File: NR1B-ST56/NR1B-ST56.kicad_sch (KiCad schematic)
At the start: 13 parts, among them J1 Conn_02x04_Odd_Even, J2 Conn_02x04_Odd_Even, J3 Conn_01x02, U1 S29GL01GP, U2 DG419LDY, X1 NUCLEO144-ZIO

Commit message: NR1B-ST56 1.0 RC 1
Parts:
- added C4: 0.1uF, Capacitor_SMD:C_0805_2012Metric, symbol Device:C
- added C5: 47uF 16V, Capacitor_SMD:CP_Elec_5x5.3, symbol Device:C_Polarized_US
- added D1, D3, D5: S1G, Diode_SMD:D_SOD-323, symbol Device:D
- added D2, D6: 15V, Diode_SMD:D_SOD-323, symbol Device:D_Zener
- added D4: 5.1V, Diode_SMD:D_SOD-323, symbol Device:D_Zener
- added FID1, FID2, FID3: Fiducial, Fiducial:Fiducial_0.5mm_Mask1mm, symbol Mechanical:Fiducial
- added R4: 1M, Resistor_SMD:R_0805_2012Metric, symbol Device:R
- added U3: OPA189ID, Package_SO:SOIC-8_3.9x4.9mm_P1.27mm, symbol NISoC-Socket:OPA189ID
- J1, J2: value Conn_02x04_Odd_Even -> 0.1" Female Long Tail
- X1: MPN (none) -> Nucleo-144; Manufacturer (none) -> ST Micro
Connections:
- net +12V: now also C4.1, D1.1 (K), D2.1 (K), U3.7 (V+); no longer J2.6 (Pin_6)
- net ANA_VWL: now also R4.1, U3.3 (+); no longer U1.14 (~{RESET})
- net EVIO: now also D5.1 (K), D6.1 (K); no longer J3.1 (Pin_1)
- net GND: now also C4.2, C5.2, D2.2 (A), D4.2 (A), D6.2 (A), R4.2, U3.4 (V-)
- net VCC: now also C5.1, D3.1 (K), D4.1 (K); no longer X1.16 (+3V3)
- new net 12V_IN: D1.2 (A), J2.6 (Pin_6)
- new net EVIO_IN: D5.2 (A), J3.1 (Pin_1)
- new net VCC_IN: D3.2 (A), X1.16 (+3V3)
- new net Vwl_buf: U1.14 (~{RESET}), U3.2 (-), U3.6
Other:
- note added: "CE Switch"
- note added: "CE switch allows for regular operation via NE1, or V read via ANA_CE."
- note added: "Connectors"
- note added: "Detector Interface"
- note added: "Forward diodes for reverse-voltage protection. Zeners for overvoltage protection."
- note added: "Jumper JP1 1-2 for VIO=VCC. Jumper JP1 2-3 for VIO=Ext. VIO Supply ext. VIO on J3"
- note added: "Optional discharge resistor"
- note added: "Power Protection"
- note added: "Vwl buffer"
- note removed: "+15V"
- note removed: "+5V"
- note removed: "-15V"
- note removed: "24V"
- note removed: "Jumper JP1 1-2 for VIO=VCC. Jumper JP1 2-3 for VIO=Vext. Supply ext. VIO on J3"
- title: NISoC Readout 1 Module Base -> NISoC Readout 1 Module - Socket TSOP-56 Bus
- moved on the sheet: C1, C2, C3, J1, J2, J3, JP1, R1, R2, R3, U1, U2A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

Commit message: Added 9V for CE#; Made global labels hierarchical
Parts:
- removed U3: OPA189ID, Package_SO:SOIC-8_3.9x4.9mm_P1.27mm, symbol NISoC-Socket:OPA189ID
- added C6: 0.33uF, Capacitor_SMD:C_0805_2012Metric, symbol Device:C
- added C7: 0.1uF, Capacitor_SMD:C_0805_2012Metric, symbol Device:C
- added D7: S1G, Diode_SMD:D_SOD-323, symbol Device:D
- added D8: 18V, Diode_SMD:D_SOD-323, symbol Device:D_Zener
- added NT1, NT2: NetTie_2, NetTie:NetTie-2_SMD_Pad0.5mm, symbol Device:NetTie_2
- added R5: 1M, Resistor_SMD:R_0805_2012Metric, symbol Device:R
- added U3: OPA2189ID, Package_SO:SOIC-8_3.9x4.9mm_P1.27mm, symbol NISoC-Socket:OPA2189ID
- added U4: NCV7800, Package_TO_SOT_SMD:TO-263-3_TabPin2, symbol NISoC-Socket:NCV7800
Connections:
- net +12V: now also U3.8 (V+)
- net ANA_CE: now also C7.1, U4.3 (OUT); no longer J1.8 (Pin_8)
- net ANA_VWL: now also NT1.1, U3.3 (+)
- net ANA_WP: now also J1.3 (Pin_3), NT2.1, R5.1, U3.5 (+); no longer J1.5 (Pin_5), U1.16 (~{WP}/ACC)
- net GND: now also C6.2, C7.2, D8.2 (A), R5.2, U3.4 (V-), U4.2 (GND)
- net +15V_IN: now reaches J2.2 (Pin_2)
- net +15V_IN: now also D7.2 (A)
- net ANA_WP_SENSE: now reaches J1.1 (Pin_1)
- net ANA_WP_SENSE: now also NT2.2
- net Vwl_buf renamed VWL_BUF
- net VWL_BUF: now also U3.1, U3.2 (-)
- new net +15V: C6.1, D7.1 (K), D8.1 (K), U4.1 (IN)
- new net ANA_VWL_SENSE: J1.5 (Pin_5), NT1.2
- new net WP_BUF: U1.16 (~{WP}/ACC), U3.6 (-), U3.7
- no-connect marks 86 -> 84
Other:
- note added: "WP buffer"
- note added: "~{CE} 9V output to enter V read mode"
- moved on the sheet: C1, C2, C3, C4, J1, J2, J3, JP1, R1, R2, R4, U2A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

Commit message: Many updates
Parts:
- removed D1: S1G, Diode_SMD:D_SOD-323, symbol Device:D
- removed D2: 15V, Diode_SMD:D_SOD-323, symbol Device:D_Zener
- added D10: 18V, Diode_SMD:D_SOD-323, symbol Device:D_Zener
- added D9: S1G, Diode_SMD:D_SOD-323, symbol Device:D
- added R6, R7: 1K, Resistor_SMD:R_0805_2012Metric, symbol Device:R
- U2: MFG 1 (none) -> Maxim; MPN 1 (none) -> DG419LDY
- U3: footprint Package_SO:SOIC-8_3.9x4.9mm_P1.27mm -> Package_SO:VSSOP-8_3.0x3.0mm_P0.65mm
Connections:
- net +12V is gone; now on net +15V: C4.1, U2.4 (V+), U3.8 (V+)
- net GND: now also D10.1 (K), R7.2; no longer C4.2, U3.4 (V-)
- net WP_BUF: now also R6.2; no longer U3.6 (-)
- net -15V_IN: now reaches J2.1 (Pin_1)
- net -15V_IN: now also D9.1 (K)
- net 12V_IN: no longer names the net of J2.6 (Pin_6)
- new net: R6.1, R7.1, U3.6 (-)
- new net -15V: C4.2, D10.2 (A), D9.2 (A), U3.4 (V-)

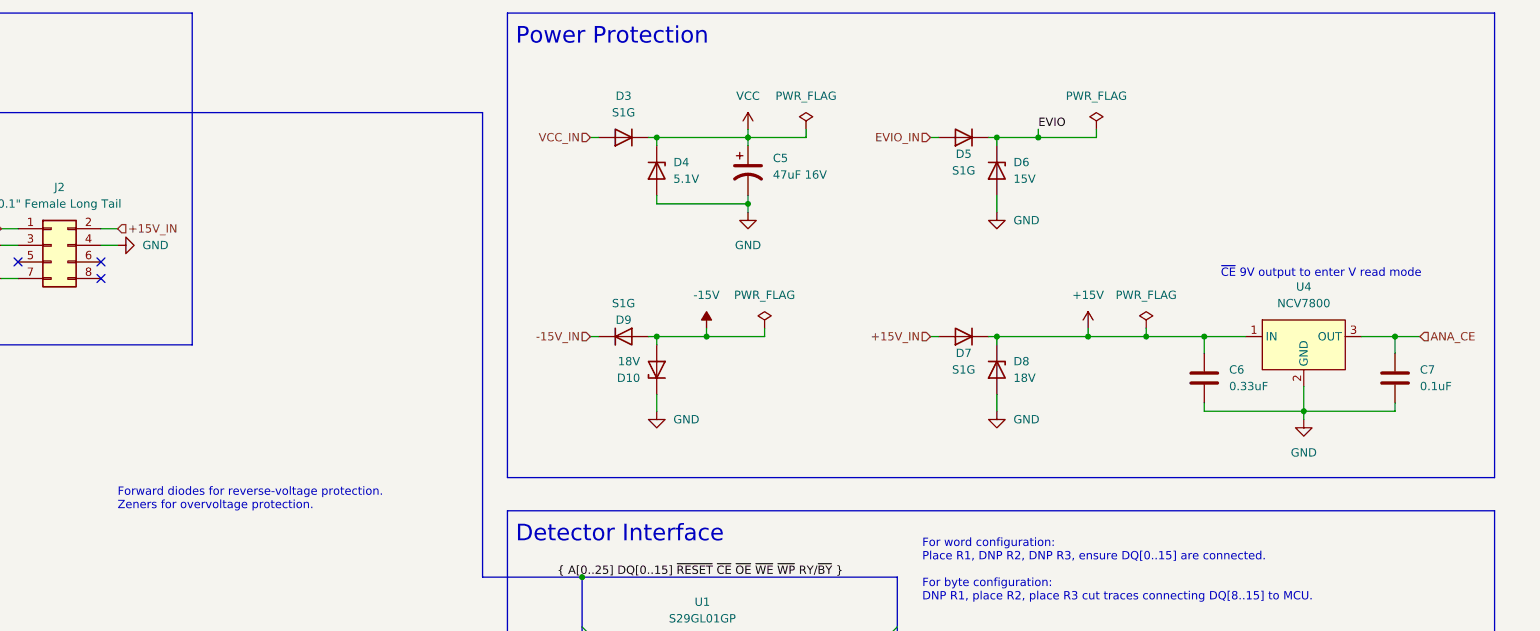
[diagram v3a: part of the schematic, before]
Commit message: Fixed footprints and silkscreen
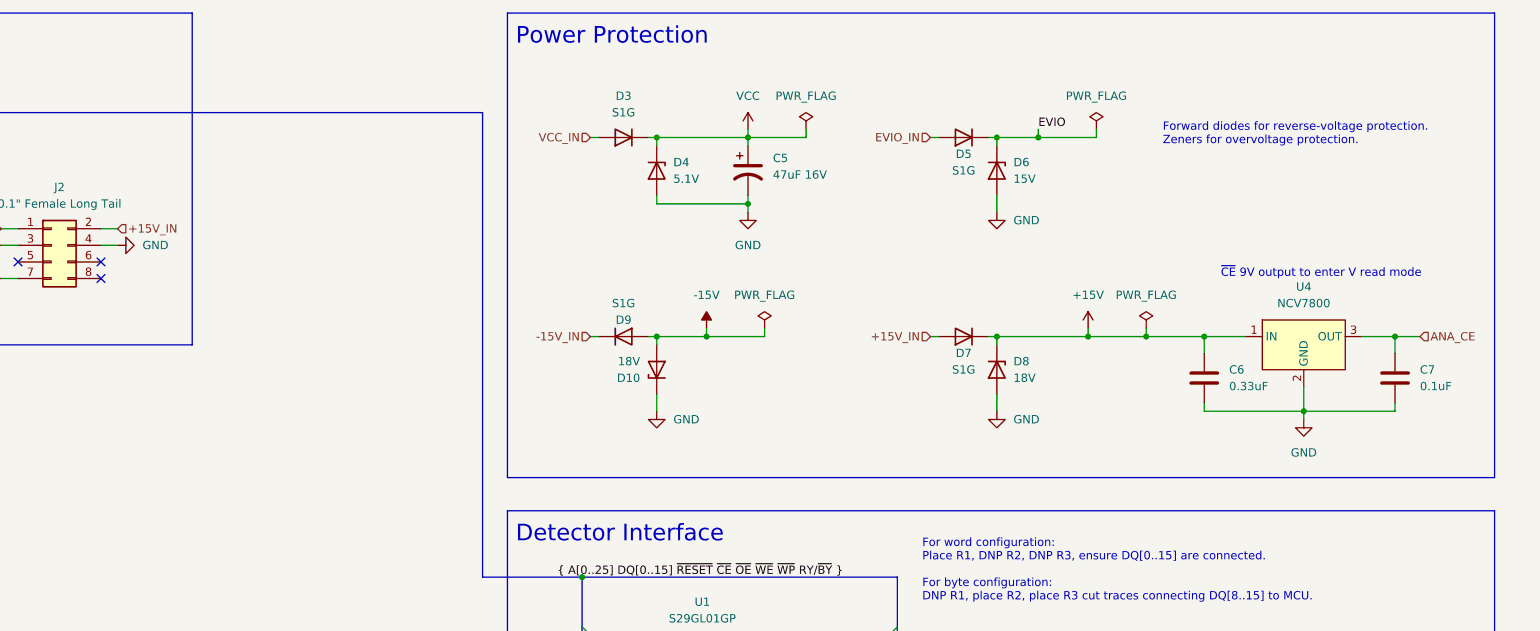
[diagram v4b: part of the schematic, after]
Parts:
- D3, D5, D7, D9: footprint Diode_SMD:D_SOD-323 -> Diode_SMD:D_SMA
- R6, R7: footprint Resistor_SMD:R_0805_2012Metric -> Resistor_SMD:R_0603_1608Metric
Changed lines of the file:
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@@
   (title_block
     (title "NISoC Readout 1 Module - Socket TSOP-56 Bus")
-    (date "2022-07-11")
+    (date "2022-08-02")
     (rev "1.0")
     (company "University of Dallas")
@@
   )
   (text "Forward diodes for reverse-voltage protection.\nZeners for overvoltage protection."
-    (at 198.12 93.98 0)
+    (at 358.14 38.1 0)
     (effects (font (size 1.27 1.27)) (justify left bottom))
   )
@@
     (property "Reference" "D3" (id 0) (at 275.59 30.48 0))
     (property "Value" "S1G" (id 1) (at 275.59 33.02 0))
-    (property "Footprint" "Diode_SMD:D_SOD-323" (id 2) (at 275.59 36.83 0)
+    (property "Footprint" "Diode_SMD:D_SMA" (id 2) (at 275.59 36.83 0)
       (effects (font (size 1.27 1.27)) hide)
     )
@@
     (property "Reference" "D5" (id 0) (at 327.66 39.37 0))
     (property "Value" "S1G" (id 1) (at 327.66 41.91 0))
-    (property "Footprint" "Diode_SMD:D_SOD-323" (id 2) (at 327.66 36.83 0)
+    (property "Footprint" "Diode_SMD:D_SMA" (id 2) (at 327.66 36.83 0)
       (effects (font (size 1.27 1.27)) hide)
     )
@@
     (property "Reference" "R6" (id 0) (at 341.63 179.07 90))
     (property "Value" "1K" (id 1) (at 341.63 173.99 90))
-    (property "Footprint" "Resistor_SMD:R_0805_2012Metric" (id 2) (at 341.63 174.752 90)
+    (property "Footprint" "Resistor_SMD:R_0603_1608Metric" (id 2) (at 341.63 174.752 90)
       (effects (font (size 1.27 1.27)) hide)
     )
@@
     (property "Reference" "D9" (id 0) (at 275.59 64.77 0))
     (property "Value" "S1G" (id 1) (at 275.59 62.23 0))
-    (property "Footprint" "Diode_SMD:D_SOD-323" (id 2) (at 275.59 67.31 0)
+    (property "Footprint" "Diode_SMD:D_SMA" (id 2) (at 275.59 67.31 0)
       (effects (font (size 1.27 1.27)) hide)
     )
@@
       (effects (font (size 1.27 1.27)) (justify left))
     )
-    (property "Footprint" "Resistor_SMD:R_0805_2012Metric" (id 2) (at 353.822 181.61 90)
+    (property "Footprint" "Resistor_SMD:R_0603_1608Metric" (id 2) (at 353.822 181.61 90)
       (effects (font (size 1.27 1.27)) hide)
     )
@@
     (property "Reference" "D7" (id 0) (at 327.66 69.85 0))
     (property "Value" "S1G" (id 1) (at 327.66 72.39 0))
-    (property "Footprint" "Diode_SMD:D_SOD-323" (id 2) (at 327.66 67.31 0)
+    (property "Footprint" "Diode_SMD:D_SMA" (id 2) (at 327.66 67.31 0)
       (effects (font (size 1.27 1.27)) hide)
     )
@@
     )
     (path "/242da293-ae6d-46dd-a6b6-d6ba3d1de6fe"
-      (reference "D3") (unit 1) (value "S1G") (footprint "Diode_SMD:D_SOD-323")
+      (reference "D3") (unit 1) (value "S1G") (footprint "Diode_SMD:D_SMA")
     )
     (path "/9b3a8a31-780a-470f-af9f-a3d21756d3b6"
@@
     )
     (path "/63e71f4d-a796-4447-8c82-09fd88a5d9bf"
-      (reference "D5") (unit 1) (value "S1G") (footprint "Diode_SMD:D_SOD-323")
+      (reference "D5") (unit 1) (value "S1G") (footprint "Diode_SMD:D_SMA")
     )
     (path "/a94e8f9e-afa6-4830-aa93-22a913360207"
@@
     )
     (path "/f299b552-8ee7-4386-9f69-6d096e2c001a"
-      (reference "D7") (unit 1) (value "S1G") (footprint "Diode_SMD:D_SOD-323")
+      (reference "D7") (unit 1) (value "S1G") (footprint "Diode_SMD:D_SMA")
     )
     (path "/61e67969-2acc-4271-bd67-f08a12f7e9a7"
@@
     )
     (path "/b0782c9b-6f78-48ad-ae89-fb24252cf241"
-      (reference "D9") (unit 1) (value "S1G") (footprint "Diode_SMD:D_SOD-323")
+      (reference "D9") (unit 1) (value "S1G") (footprint "Diode_SMD:D_SMA")
     )
     (path "/c7a096df-9a13-41ae-ae08-3eb578cfc15d"
@@
     )
     (path "/ad5cafb3-1aba-4113-8611-9bc359308370"
-      (reference "R6") (unit 1) (value "1K") (footprint "Resistor_SMD:R_0805_2012Metric")
+      (reference "R6") (unit 1) (value "1K") (footprint "Resistor_SMD:R_0603_1608Metric")
     )
     (path "/de0b3ff5-56b8-4e0c-af8a-6e6e370d3733"
-      (reference "R7") (unit 1) (value "1K") (footprint "Resistor_SMD:R_0805_2012Metric")
+      (reference "R7") (unit 1) (value "1K") (footprint "Resistor_SMD:R_0603_1608Metric")
     )
     (path "/65a157dc-e557-41fa-933f-a1426617469b"

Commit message: Added 0ohm resistors to DQ8-15 lines, updated mode instructions
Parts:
- added R10, R11, R12, R13, R14, R15, R8, R9: 0, Resistor_SMD:R_0603_1608Metric, symbol Device:R
- R1, R2, R3: footprint Resistor_SMD:R_0805_2012Metric -> Resistor_SMD:R_0603_1608Metric
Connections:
- net DQ10: now also R10.1; no longer X1.127 (PE13)
- net DQ11: now also R11.2; no longer X1.123 (PE14)
- net DQ12: now also R12.1; no longer X1.125 (PE15)
- net DQ13: now also R13.2; no longer X1.82 (STLINK_TX/PD8)
- net DQ14: now also R14.1; no longer X1.69 (STLINK_RX/PD9)
- net DQ15: now also R15.2; no longer X1.137 (PD10)
- net DQ8: now also R8.1; no longer X1.128 (PE11)
- net DQ9: now also R9.2; no longer X1.121 (PE12)
- new net: R15.1, X1.137 (PD10)
- new net: R13.1, X1.82 (STLINK_TX/PD8)
- new net: R14.2, X1.69 (STLINK_RX/PD9)
- new net: R11.1, X1.123 (PE14)
- new net: R9.1, X1.121 (PE12)
- new net: R12.2, X1.125 (PE15)
- new net: R10.2, X1.127 (PE13)
- new net: R8.2, X1.128 (PE11)
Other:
- note added: "For word configuration: Place R1, DNP R2, DNP R3, place R8 - R13. For byte configuration: DNP R1, place R2, place R3, DNP R8 - R13."
- note removed: "For word configuration: Place R1, DNP R2, DNP R3, ensure DQ[0..15] are connected. For byte configuration: DNP R1, place R2, place R3 cut traces connecting DQ[8..15] to MCU."
- moved on the sheet: C3, J1, J2, U2A, U2B

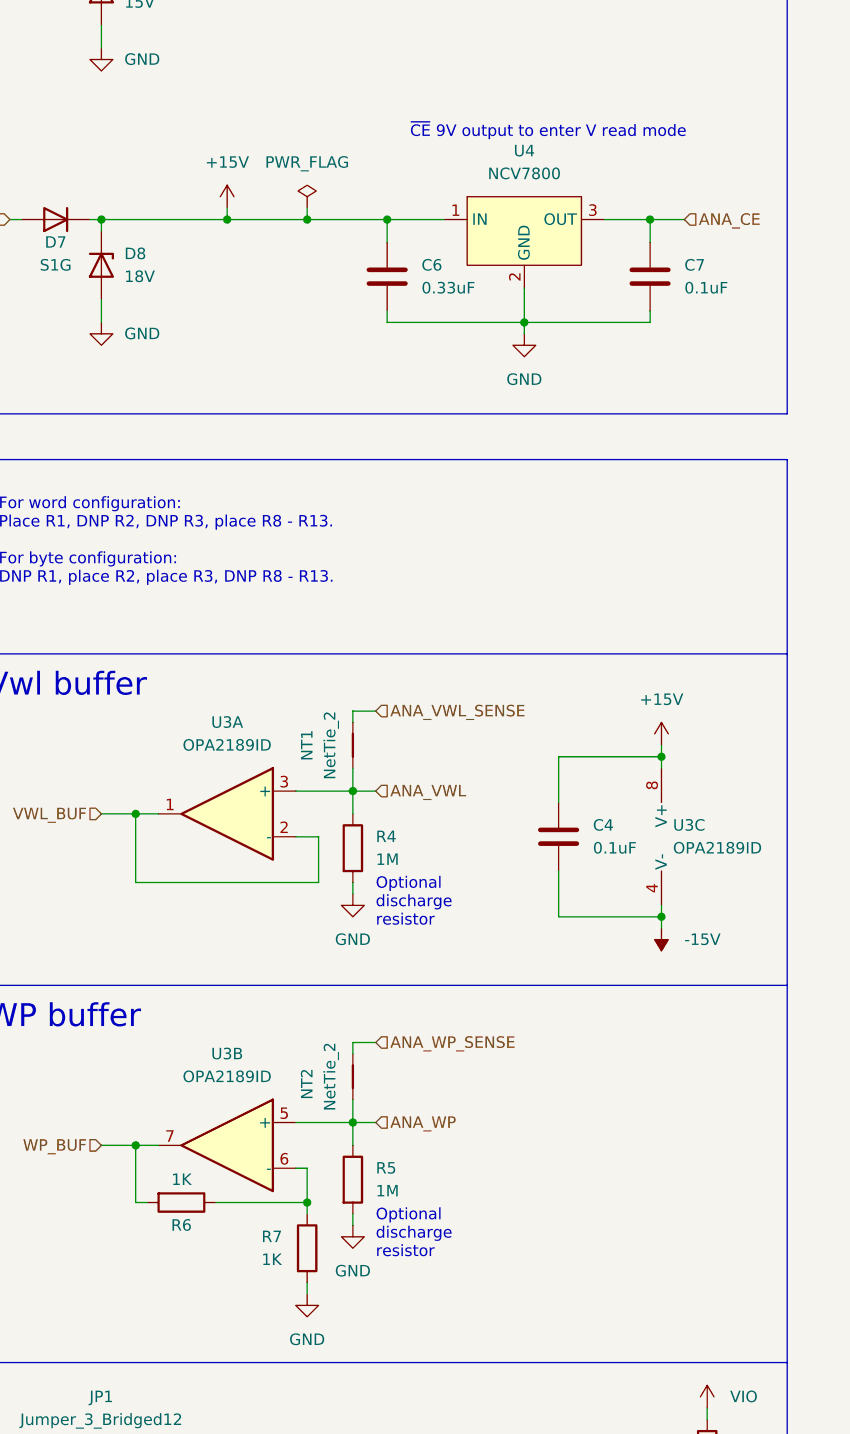
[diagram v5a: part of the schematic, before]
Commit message: Replaced dual op amp with two single op amps
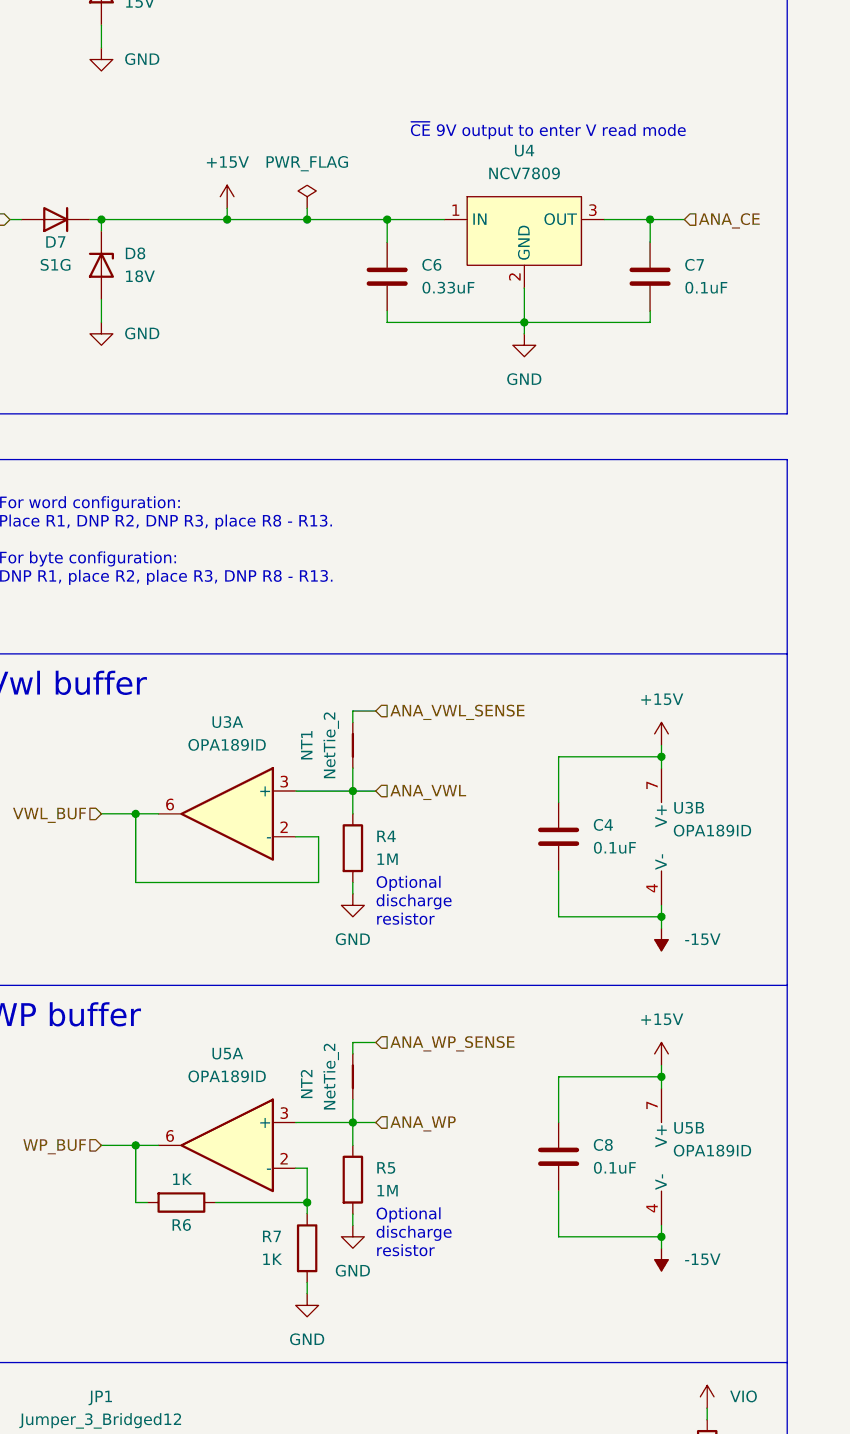
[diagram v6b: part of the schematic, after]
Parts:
- removed U3: OPA2189ID, Package_SO:VSSOP-8_3.0x3.0mm_P0.65mm, symbol NISoC-Socket:OPA2189ID
- added C8: 0.1uF, Capacitor_SMD:C_0805_2012Metric, symbol Device:C
- added U3, U5: OPA189ID, Package_SO:SOIC-8_3.9x4.9mm_P1.27mm, symbol NISoC-Socket:OPA189ID
- U4: value NCV7800 -> NCV7809
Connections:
- net +15V: now also C8.1, U3.7 (V+), U5.7 (V+)
- net -15V: now also C8.2, U3.4 (V-), U5.4 (V-)
- net ANA_VWL: now also U3.3 (+)
- net ANA_WP: now also U5.3 (+)
- net VWL_BUF: now also U3.2 (-), U3.6
- net WP_BUF: now also U5.6
- net at R6.1, R7.1: now also U5.2 (-)
